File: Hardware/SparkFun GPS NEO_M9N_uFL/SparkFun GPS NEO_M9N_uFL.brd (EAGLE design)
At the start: 40.6 x 33 mm, 94 parts, among them J13 U.FL, J2 Qwiic Right Angle, J4 Qwiic Right Angle, U1 U-BLOX_NEO-M9N, U2 3.3V

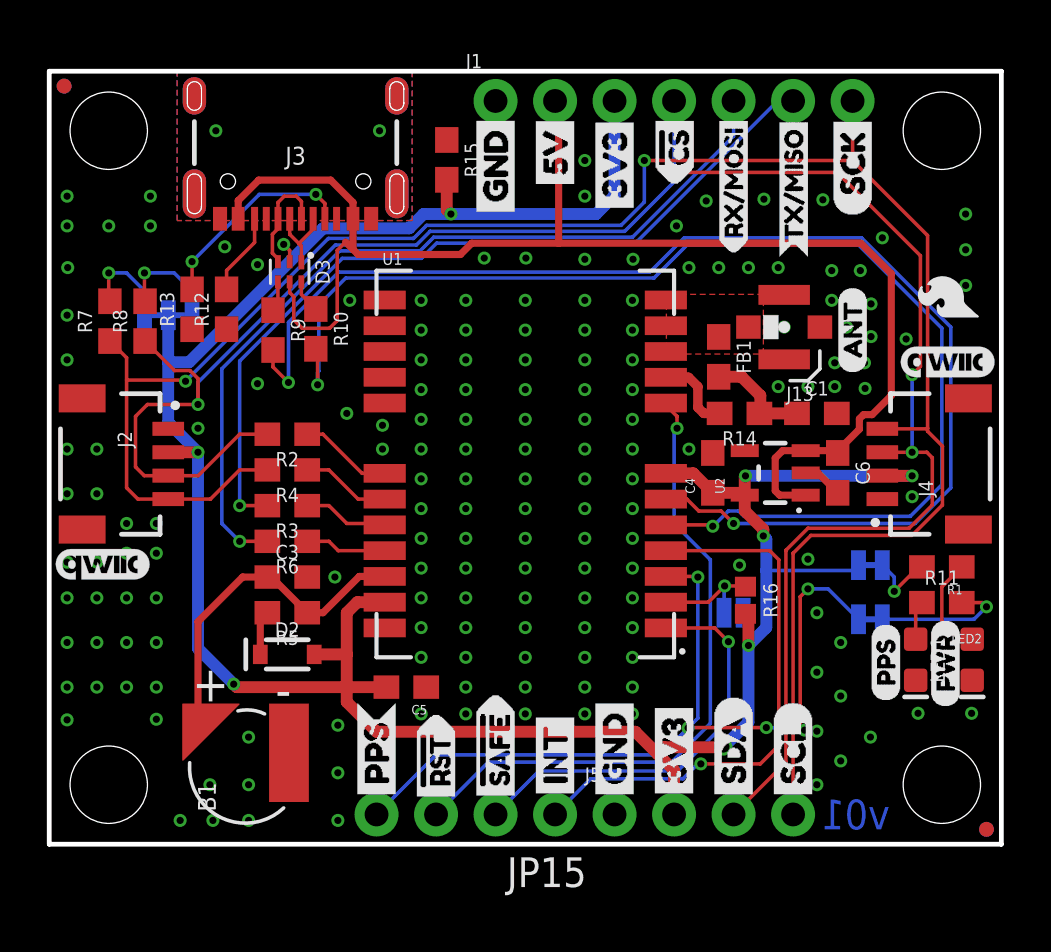
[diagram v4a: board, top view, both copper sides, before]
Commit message: Fixes 5V line, changes version
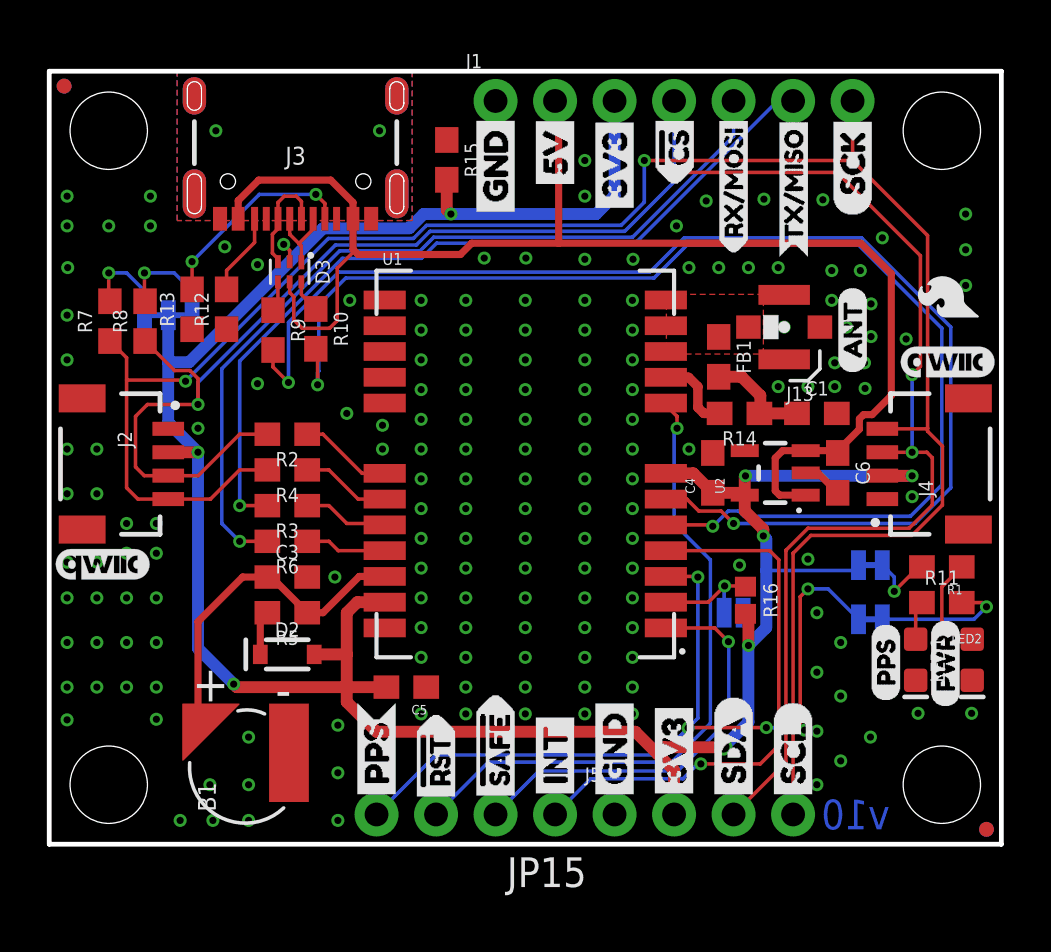
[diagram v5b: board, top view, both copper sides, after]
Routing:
- net 5V: track 60.7 -> 60.0 mm
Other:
- board text added: "v10"
- board text removed: "v01"
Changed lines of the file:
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@@
 <wire x1="40.64" y1="32.9946" x2="40.64" y2="0" width="0.2032" layer="20"/>
 <wire x1="40.64" y1="0" x2="0" y2="0" width="0.2032" layer="20"/>
-<text x="34.417" y="1.27" size="1.27" layer="16" font="vector" ratio="15" rot="MR180" align="center">v01</text>
+<text x="34.417" y="1.27" size="1.27" layer="16" font="vector" ratio="15" rot="MR180" align="center">v10</text>
 <text x="-2.54" y="-8.89" size="1.778" layer="47">Measurements in inches</text>
 <dimension x1="0" y1="0" x2="0" y2="33.02" x3="-7.62" y3="16.51" textsize="1.778" textratio="15" layer="47" unit="inch"/>
@@
 <wire x1="21.7424" y1="31.5722" x2="21.59" y2="31.7246" width="0.3048" layer="1"/>
 <wire x1="21.7424" y1="31.5722" x2="21.7424" y2="25.654" width="0.3048" layer="1"/>
-<wire x1="12.6481" y1="25.7059" x2="12.9656" y2="25.3884" width="0.3048" layer="1"/>
 <wire x1="12.9656" y1="25.3884" x2="13.1826" y2="25.1714" width="0.3048" layer="1"/>
 <wire x1="12.9656" y1="25.3884" x2="12.9656" y2="26.6938" width="0.3048" layer="1"/>
-<wire x1="12.2925" y1="25.3503" x2="12.6481" y2="25.7059" width="0.1524" layer="1"/>
-<wire x1="12.2925" y1="22.3509" x2="12.2925" y2="25.3503" width="0.1524" layer="1"/>
+<wire x1="12.2925" y1="22.3509" x2="12.2925" y2="24.5883" width="0.1524" layer="1"/>
 <wire x1="13.1826" y1="25.1714" x2="17.5514" y2="25.1714" width="0.3048" layer="1"/>
 <wire x1="17.5514" y1="25.1714" x2="18.034" y2="25.654" width="0.3048" layer="1"/>
 <wire x1="18.034" y1="25.654" x2="21.7424" y2="25.654" width="0.3048" layer="1"/>
+<wire x1="12.9656" y1="25.2614" x2="12.9656" y2="25.3884" width="0.1524" layer="1"/>
+<wire x1="12.2925" y1="24.5883" x2="12.9656" y2="25.2614" width="0.1524" layer="1"/>
 </signal>
 <signal name="N$11">

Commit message: Moves production files around
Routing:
- net GND: vias 171 -> 170
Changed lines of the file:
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@@
 <via x="32.385" y="12.1666" extent="1-16" drill="0.3048"/>
 <via x="32.766" y="7.3406" extent="1-16" drill="0.3048"/>
-<via x="32.766" y="4.826" extent="1-16" drill="0.3048"/>
 <via x="15.875" y="9.2456" extent="1-16" drill="0.3048"/>
 <via x="17.78" y="9.2456" extent="1-16" drill="0.3048"/>

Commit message: Removes local eagle library and replaces part from that library with part from SparkFun Eagle Library
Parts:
- U1: device gps:NEO-M9N -> SparkFun-GPS:NEO-M9N
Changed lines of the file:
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@@
 <?xml version="1.0" encoding="utf-8"?>
 <!DOCTYPE eagle SYSTEM "eagle.dtd">
-<eagle version="9.4.2">
+<eagle version="9.5.1">
 <drawing>
 <settings>
@@
 <element name="U$37" library="buzzard_labels (36)" package="TX#MISO1" value="" x="31.7754" y="24.0284" smashed="yes" rot="MR90"/>
 <element name="LOGO2" library="SparkFun-Aesthetics" package="SFE_LOGO_NAME_FLAME_.1" value="SFE_LOGO_NAME_FLAME.1_INCH" x="20.193" y="20.6756" smashed="yes" rot="MR0"/>
-<element name="U1" library="gps" package="NEO-M9N" value="U-BLOX_NEO-M9N" x="20.32" y="16.2306" smashed="yes">
+<element name="U1" library="SparkFun-GPS" package="NEO-M9N" value="U-BLOX_NEO-M9N" x="20.32" y="16.2306" smashed="yes">
 <attribute name="NAME" x="14.22" y="24.7306" size="0.508" layer="25"/>
 <attribute name="PROD_ID" value="IC-14651" x="20.32" y="16.2306" size="1.778" layer="27" display="off"/>
